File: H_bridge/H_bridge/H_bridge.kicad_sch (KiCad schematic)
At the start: 17 parts, among them J1 Screw_Terminal_01x02, J2 Screw_Terminal_01x06, J3 Pins_02x10_P1.27mm_TH, U1 VNH7040AYTR

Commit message: puente H, Done
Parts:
- added C2: 470uF, Capacitor_SMD:CP_Elec_10x14.3, symbol Device:C_US
- added C4: 100nF, PCM_Capacitor_SMD_AKL:C_0805_2012Metric, symbol PCM_Capacitor_AKL:C_0805
- C1: V (none) -> 10V
- U1: footprint UL_Hbridge:POWERSSO-36TP_STM-M -> UL_Full_H_Bridge_SMD:POWERSSO-36TP_STM-M
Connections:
- net +24V: now also C2.1, C4.1
- net CS/DF_EN: now also R4.2; no longer R6.2
- net GND: now also C2.2, C4.2
- net INA: now also R2.2; no longer R1.2
- net INB: now also R5.2; no longer R2.2
- net SEL0: now also R1.2; no longer R4.2
- net SEL1: now also R6.2; no longer R5.2
- net at R5.1: now also J3.12; no longer J3.10
- net at C1.1, R7.1: now also J3.8; no longer J3.14
- net at R4.1: now also J3.10; no longer J3.8
- net at R6.1: now also J3.14; no longer J3.12
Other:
- note added: "ALIMENTACION"
- moved on the sheet: C1, J1, J3, R1, R2, R3, R4, R5, R6, R7, R8

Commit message: avances pcb
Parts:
- removed J2: Screw_Terminal_01x06, TerminalBlock:TerminalBlock_MaiXu_MX126-5.0-06P_1x06_P5.00mm, symbol Connector:Screw_Terminal_01x06
- added J4: Screw_Terminal_01x02, TerminalBlock_4Ucon:TerminalBlock_4Ucon_1x02_P3.50mm_Horizontal, symbol Connector:Screw_Terminal_01x02
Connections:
- net +24V: now also U1.37 (Heat_sink)
- net Drain_Low_SideA: now also U1.38 (Heat_sink), J4.2 (Pin_2)
- net Drain_Low_SideB: now also U1.39 (Heat_sink), J4.1 (Pin_1)
- removed net Heatsink: U1.37 (Heat_sink), U1.38 (Heat_sink), U1.39 (Heat_sink)
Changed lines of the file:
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@@
 	(rectangle
 		(start 96.52 55.88)
-		(end 198.12 130.81)
+		(end 198.12 142.24)
 		(stroke
 			(width 1)
@@
 	)
 	(junction
-		(at 143.51 128.27)
-		(diameter 0)
-		(color 0 0 0 0)
-	)
-	(junction
 		(at 172.72 87.63)
 		(diameter 0)
@@
 	)
 	(junction
-		(at 146.05 128.27)
-		(diameter 0)
-		(color 0 0 0 0)
-	)
-	(junction
 		(at 168.91 102.87)
 		(diameter 0)
@@
 	(wire
 		(pts
+			(xy 146.05 134.62) (xy 146.05 128.27)
+		)
+		(stroke
+			(width 0)
+			(type default)
+		)
+	)
+	(wire
+		(pts
 			(xy 22.86 48.26) (xy 22.86 49.53)
 		)
@@
 	(wire
 		(pts
+			(xy 137.16 128.27) (xy 140.97 128.27)
+		)
+		(stroke
+			(width 0)
+			(type default)
+		)
+	)
+	(wire
+		(pts
 			(xy 119.38 85.09) (xy 124.46 85.09)
 		)
@@
 	(wire
 		(pts
+			(xy 142.24 134.62) (xy 146.05 134.62)
+		)
+		(stroke
+			(width 0)
+			(type default)
+		)
+	)
+	(wire
+		(pts
 			(xy 102.87 100.33) (xy 120.65 100.33)
 		)
@@
 	(wire
 		(pts
-			(xy 143.51 128.27) (xy 146.05 128.27)
-		)
-		(stroke
-			(width 0)
-			(type default)
-		)
-	)
-	(wire
-		(pts
 			(xy 119.38 87.63) (xy 119.38 85.09)
 		)
@@
 	(wire
 		(pts
-			(xy 146.05 128.27) (xy 148.59 128.27)
-		)
-		(stroke
-			(width 0)
-			(type default)
-		)
-	)
-	(wire
-		(pts
 			(xy 48.26 38.1) (xy 57.15 38.1)
 		)
@@
 	(wire
 		(pts
-			(xy 140.97 128.27) (xy 143.51 128.27)
+			(xy 62.23 33.02) (xy 60.96 33.02)
 		)
 		(stroke
@@
 	(wire
 		(pts
-			(xy 62.23 33.02) (xy 60.96 33.02)
+			(xy 168.91 82.55) (xy 172.72 82.55)
 		)
 		(stroke
@@
 	(wire
 		(pts
-			(xy 168.91 82.55) (xy 172.72 82.55)
+			(xy 22.86 33.02) (xy 22.86 35.56)
 		)
 		(stroke
@@
 	(wire
 		(pts
-			(xy 22.86 33.02) (xy 22.86 35.56)
+			(xy 143.51 128.27) (xy 143.51 132.08)
 		)
 		(stroke
@@
 	(wire
 		(pts
+			(xy 142.24 132.08) (xy 143.51 132.08)
+		)
+		(stroke
+			(width 0)
+			(type default)
+		)
+	)
+	(wire
+		(pts
 			(xy 35.56 40.64) (xy 40.64 40.64)
 		)
@@
 		)
 	)
+	(label "Drain_Low_SideA"
+		(at 142.24 132.08 180)
+		(effects
+			(font
+				(size 1.27 1.27)
+			)
+			(justify right bottom)
+		)
+	)
 	(label "INB"
 		(at 57.15 38.1 180)
@@
 	)
 	(label "Drain_Low_SideB"
+		(at 142.24 134.62 180)
+		(effects
+			(font
+				(size 1.27 1.27)
+			)
+			(justify right bottom)
+		)
+	)
+	(label "Drain_Low_SideB"
 		(at 186.69 92.71 180)
 		(effects
@@
 		)
 	)
-	(global_label "Heatsink"
-		(shape passive)
-		(at 148.59 128.27 0)
-		(fields_autoplaced yes)
-		(effects
-			(font
-				(size 1.27 1.27)
-			)
-			(justify left)
-		)
-		(property "Intersheetrefs" "${INTERSHEET_REFS}"
-			(at 158.5677 128.27 0)
-			(effects
-				(font
-					(size 1.27 1.27)
-				)
-				(justify left)
-				(hide yes)
-			)
-		)
-	)
 	(symbol
 		(lib_id "power:+24V")
@@
 	)
 	(symbol
+		(lib_id "power:+24V")
+		(at 137.16 128.27 90)
+		(unit 1)
+		(exclude_from_sim no)
+		(in_bom yes)
+		(on_board yes)
+		(dnp no)
+		(property "Reference" "#PWR015"
+			(at 140.97 128.27 0)
+			(effects
+				(font
+					(size 1.27 1.27)
+				)
+				(hide yes)
+			)
+		)
+		(property "Value" "+24V"
+			(at 140.97 127 90)
+			(effects
+				(font
+					(size 1.27 1.27)
+				)
+				(justify left)
+			)
+		)
+		(property "Footprint" ""
+			(at 137.16 128.27 0)
+			(effects
+				(font
+					(size 1.27 1.27)
+				)
+				(hide yes)
+			)
+		)
+		(property "Datasheet" ""
+			(at 137.16 128.27 0)
+			(effects
+				(font
+					(size 1.27 1.27)
+				)
+				(hide yes)
+			)
+		)
+		(property "Description" "Power symbol creates a global label with name \"+24V\""
+			(at 137.16 128.27 0)
+			(effects
+				(font
+					(size 1.27 1.27)
+				)
+				(hide yes)
+			)
+		)
+		(pin "1"
+		)
+		(instances
+			(project "H_bridge"
+				(path "/f44802e2-8b3d-47f8-8c3e-4de3fa2035af"
+					(reference "#PWR015")
+					(unit 1)
+				)
+			)
+		)
+	)
+	(symbol
 		(lib_id "PCM_Resistor_US_AKL:R_0603")
 		(at 43.18 30.48 90)
@@
 	)
 	(symbol
+		(lib_id "Connector:Screw_Terminal_01x02")
+		(at 26.67 67.31 180)
+		(unit 1)
+		(exclude_from_sim no)
+		(in_bom yes)
+		(on_board yes)
+		(dnp no)
+		(property "Reference" "J4"
+			(at 22.86 67.31 0)
+			(effects
+				(font
+					(size 1.27 1.27)
+				)
+			)
+		)
+		(property "Value" "Screw_Terminal_01x02"
+			(at 45.72 59.69 0)
+			(effects
+				(font
+					(size 1.27 1.27)
+				)
+				(hide yes)
+			)
+		)
+		(property "Footprint" "TerminalBlock_4Ucon:TerminalBlock_4Ucon_1x02_P3.50mm_Horizontal"
+			(at 26.67 67.31 0)
+			(effects
+				(font
+					(size 1.27 1.27)
+				)
+				(hide yes)
+			)
+		)
+		(property "Datasheet" "~"
+			(at 26.67 67.31 0)
+			(effects
+				(font
+					(size 1.27 1.27)
+				)
+				(hide yes)
+			)
+		)
+		(property "Description" "Generic screw terminal, single row, 01x02, script generated (kicad-library-utils/schlib/autogen/connector/)"
+			(at 26.67 67.31 0)
+			(effects
+				(font
+					(size 1.27 1.27)
+				)
+				(hide yes)
+			)
+		)
+		(pin "1"
+		)
+		(pin "2"
+		)
+		(instances
+			(project "H_bridge"
+				(path "/f44802e2-8b3d-47f8-8c3e-4de3fa2035af"
+					(reference "J4")
+					(unit 1)
+				)
+			)
+		)
+	)
+	(symbol
 		(lib_id "PCM_Resistor_US_AKL:R_0603")
 		(at 66.04 33.02 90)
@@
 					(unit 1)
 				)
-			)
-		)
-	)
-	(symbol
-		(lib_id "Connector:Screw_Terminal_01x06")
-		(at 26.67 69.85 0)
-		(mirror y)
-		(unit 1)
-		(exclude_from_sim no)
-		(in_bom yes)
-		(on_board yes)
-		(dnp no)
-		(property "Reference" "J2"
-			(at 22.86 69.85 0)
-			(effects
-				(font
-					(size 1.27 1.27)
-				)
-			)
-		)
-		(property "Value" "Screw_Terminal_01x06"
-			(at 44.45 81.28 0)
-			(effects
-				(font
-					(size 1.27 1.27)
-				)
-				(hide yes)
-			)
-		)
-		(property "Footprint" "TerminalBlock:TerminalBlock_MaiXu_MX126-5.0-06P_1x06_P5.00mm"
-			(at 26.67 69.85 0)
-			(effects
-				(font
-					(size 1.27 1.27)
-				)
-				(hide yes)
-			)
-		)
-		(property "Datasheet" "~"
-			(at 26.67 69.85 0)
-			(effects
-				(font
-					(size 1.27 1.27)
-				)
-				(hide yes)
-			)
-		)
-		(property "Description" "Generic screw terminal, single row, 01x06, script generated (kicad-library-utils/schlib/autogen/connector/)"
-			(at 26.67 69.85 0)
-			(effects
-				(font
-					(size 1.27 1.27)
-				)
-				(hide yes)
-			)
-		)
-		(pin "2"
-		)
-		(pin "4"
-		)
-		(pin "6"
-		)
-		(pin "1"
-		)
-		(pin "5"
-		)
-		(pin "3"
-		)
-		(instances
-			(project ""
-				(path "/f44802e2-8b3d-47f8-8c3e-4de3fa2035af"
-					(reference "J2")
-					(unit 1)
-				)

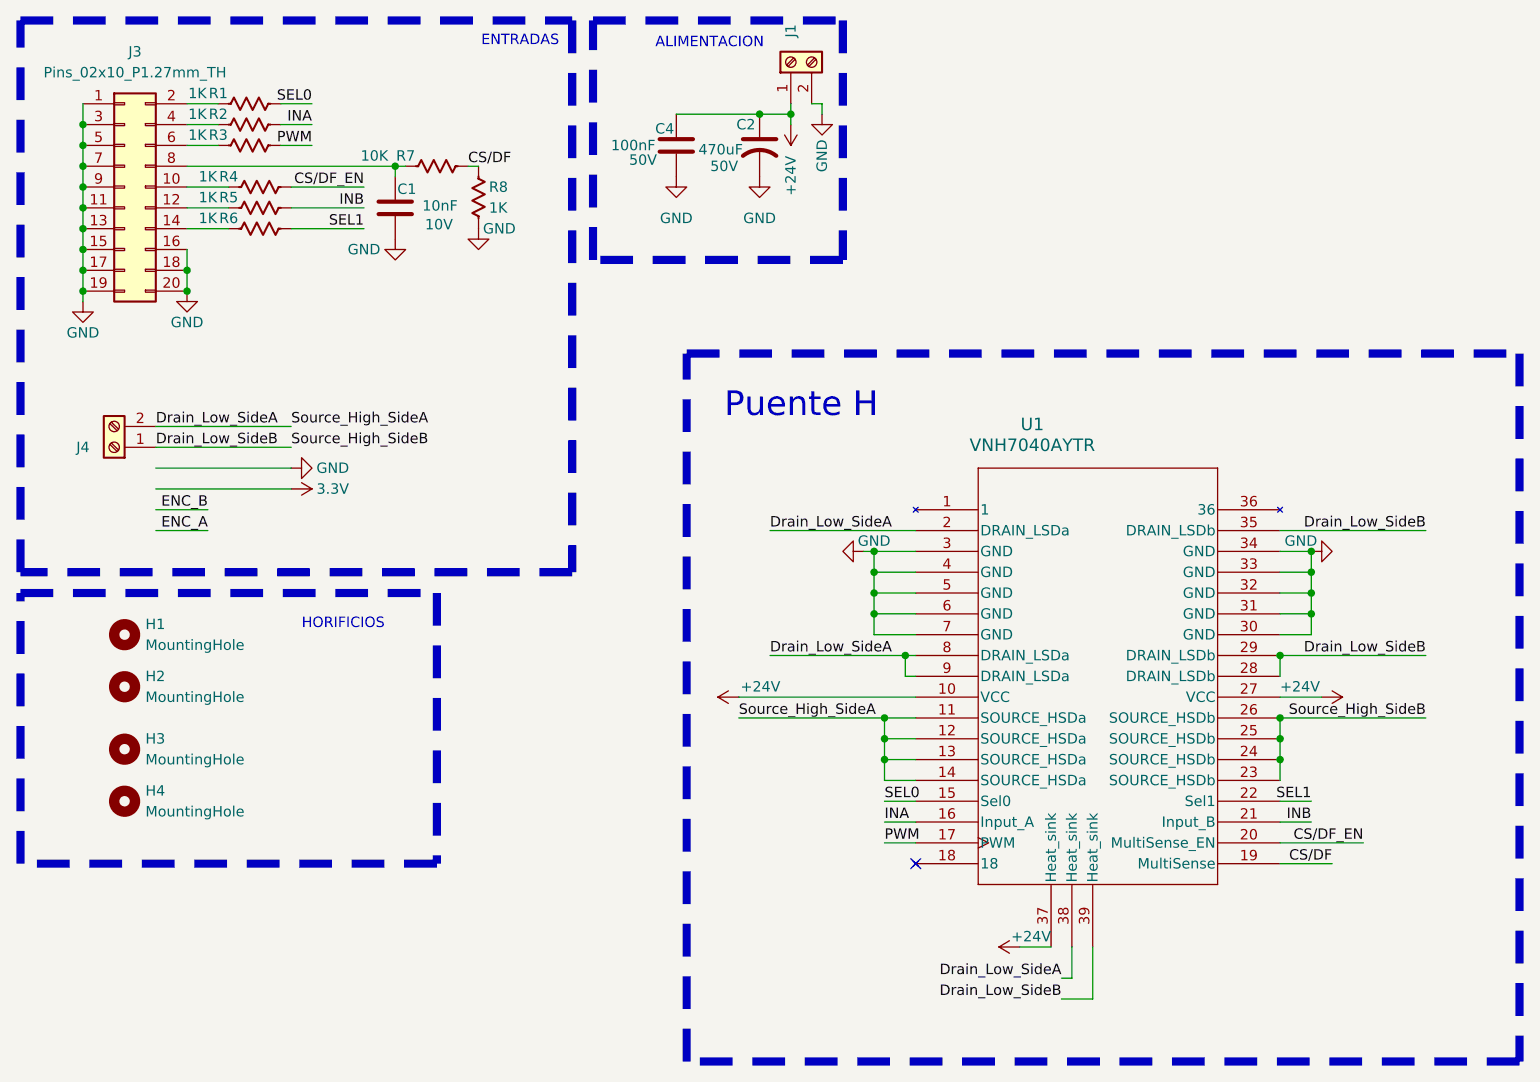
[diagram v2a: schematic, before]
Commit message: Puente H Done
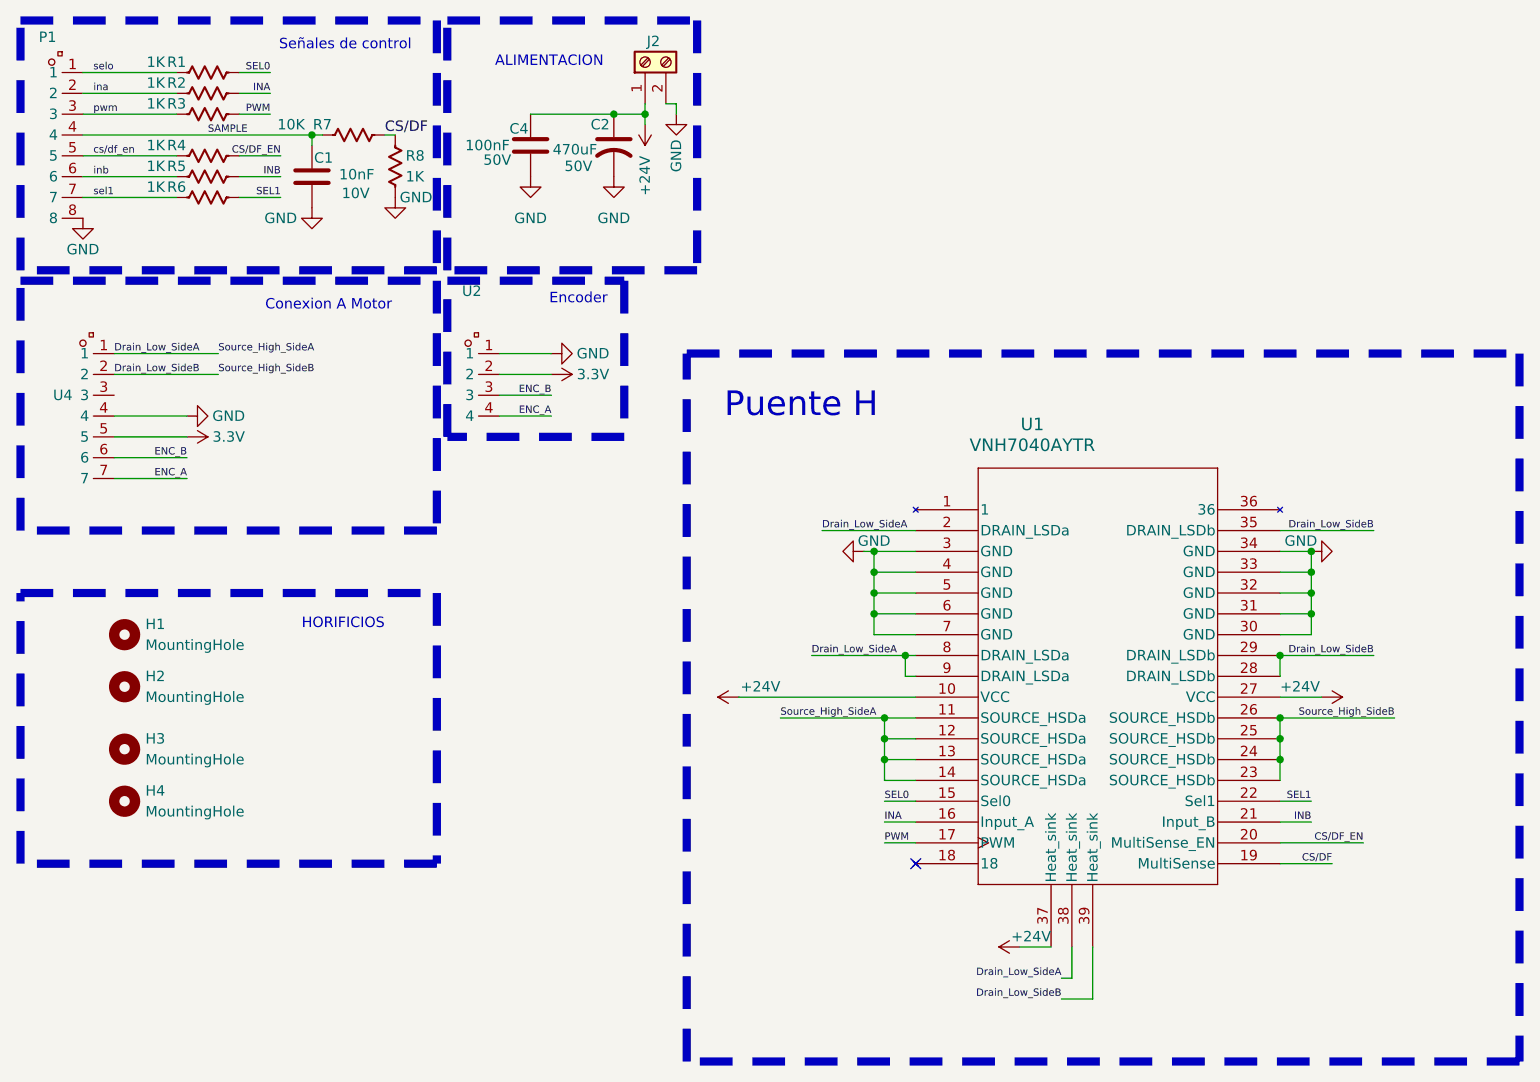
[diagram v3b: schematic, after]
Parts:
- removed J1, J4: Screw_Terminal_01x02, TerminalBlock_4Ucon:TerminalBlock_4Ucon_1x02_P3.50mm_Horizontal, symbol Connector:Screw_Terminal_01x02
- removed J3: Pins_02x10_P1.27mm_TH, Connector_IDC:IDC-Header_2x10_P2.54mm_Vertical, symbol PCM_4ms_Connector:Pins_02x10_P1.27mm_TH
- added J2: Screw_Terminal_01x02, TerminalBlock_4Ucon:TerminalBlock_4Ucon_1x02_P3.50mm_Horizontal, symbol Connector:Screw_Terminal_01x02
- added P1: Header-Female-2.54_1x8, EasyEDA:HDR-TH_8P-P2.54-V-F_2, symbol EasyEDA:Header-Female-2.54_1x8
- added U2: HX PZ2.54-1X4P ZZ, EasyEDA:HDR-TH_4P-P2.54-V-M, symbol EasyEDA:HXPZ2.54-1X4PZZ
- added U4: DB125-3.5-7P-GN-S, EasyEDA:CONN-TH_7P-P3.50_DORABO_DB125-3.5-7P-GN-S, symbol EasyEDA:DB125-3.5-7P-GN-S
- H1, H2, H3, H4: footprint MountingHole:MountingHole_3.2mm_M3 -> MountingHole:MountingHole_2.2mm_M2
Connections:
- net +24V: now also J2.1 (Pin_1)
- net 3.3V: now also U2.2, U4.5
- net Drain_Low_SideA: now also U4.1
- net Drain_Low_SideB: now also U4.2
- net ENC_A: now also U2.4, U4.7
- net ENC_B: now also U2.3, U4.6
- net GND: now also J2.2 (Pin_2), P1.8, U2.1, U4.4
- net inb: now reaches R5.1
- net inb: now also P1.6
- net pwm: now reaches R3.1
- net pwm: now also P1.3
- net ina: now reaches R2.1
- net ina: now also P1.2
- net SAMPLE: now reaches C1.1, R7.1
- net SAMPLE: now also P1.4
- net cs/df_en: now reaches R4.1
- net cs/df_en: now also P1.5
- net sel1: now reaches R6.1
- net sel1: now also P1.7
- net selo: now reaches R1.1
- net selo: now also P1.1
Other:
- note added: "Conexion A Motor"
- note added: "Encoder"
- note added: "Señales de control"
- note removed: "ENTRADAS"
- moved on the sheet: C1, C2, C4, R1, R2, R3, R4, R5, R6, R7, R8
